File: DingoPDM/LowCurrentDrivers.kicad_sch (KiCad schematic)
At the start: 0 parts

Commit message: V5 As Built
-Changed ADS1015 to MAX11613EUA+T due to supply issues
-Changed PCB to match JLCPCB 2oz rules
-Changed ON_SW input to 12V switched
-Switched to TagConnect TC2030
-Changed pin positions of GND, IN1, IN2
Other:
- title: (none) -> Dingo_PDM
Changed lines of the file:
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@@
 (kicad_sch (version 20230121) (generator eeschema)
   (paper "A4")
+  (title_block
+    (title "Dingo_PDM")
+    (date "2023-02-23")
+    (rev "v5")
+    (comment 3 "github.com/corygrant")
+    (comment 4 "Cory Grant")
+  )
   (wire (pts (xy 52.07 74.93) (xy 57.15 74.93))
     (stroke (width 0) (type default))
@@
     (instances
       (project "DingoPDM"
-        (path "/8948e307-9174-4227-9c28-3ff885e6e83d/00000000-0000-0000-0000-00005f54bf48" (page "9"))
-      )
-    )
+        (path "/8948e307-9174-4227-9c28-3ff885e6e83d/00000000-0000-0000-0000-00005f54bf48" (page "13"))
+      )
+    )

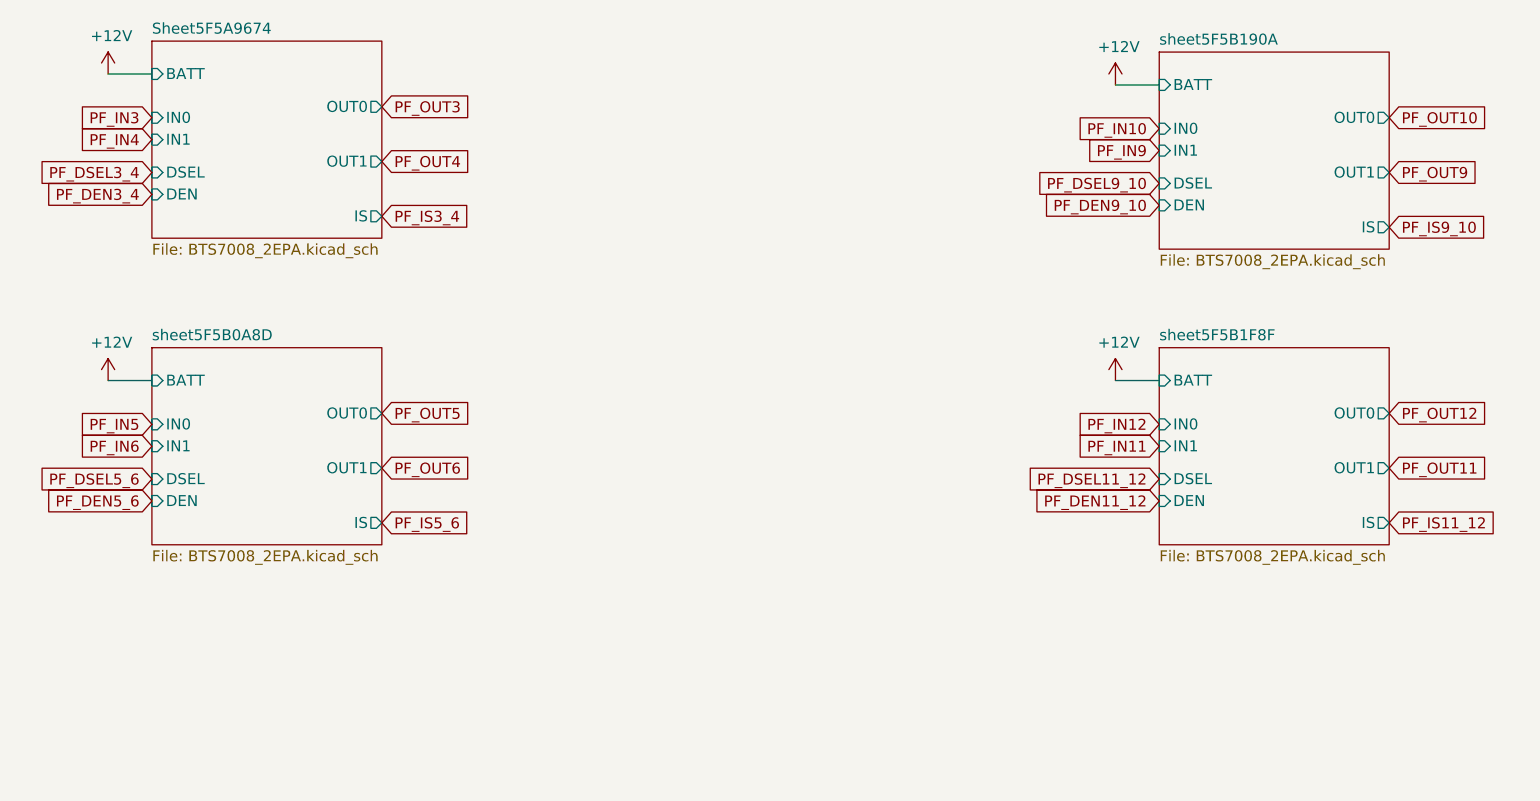
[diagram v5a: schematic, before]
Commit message: Redesigned to a smaller unit
4x high current, 2x med current, 4x low current, 2x digital inputs
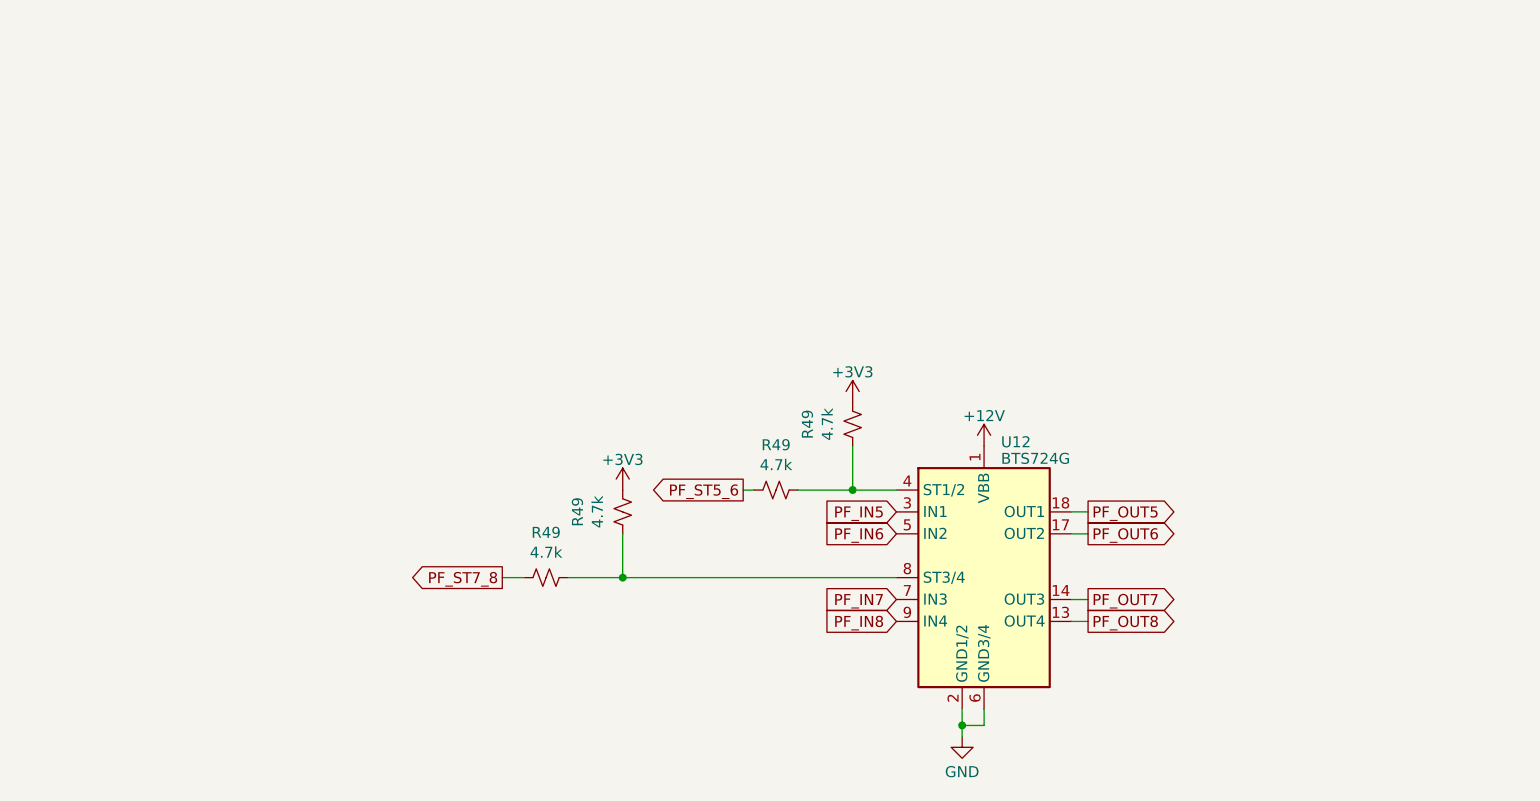
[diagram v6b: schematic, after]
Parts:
- added R49 (x4): 4.7k, Resistor_SMD:R_0805_2012Metric, symbol Device:R_Small_US
- added U12: BTS724G, Package_SO:Infineon_PG-DSO-20-32, symbol Power_Management:BTS724G
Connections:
- net +12V: now also U12.1 (VBB), U12.10 (VBB), U12.11 (VBB), U12.12 (VBB), U12.15 (VBB), U12.16 (VBB), U12.19 (VBB), U12.20 (VBB)
- net PF_IN5: now also U12.3 (IN1)
- net PF_IN6: now also U12.5 (IN2)
- net PF_OUT5: now also U12.18 (OUT1)
- net PF_OUT6: now also U12.17 (OUT2)
- new net: R49.1, R49.2, U12.8 (ST3/4)
- new net: R49.1, R49.2, U12.4 (ST1/2)
- new net +3V3: R49.1, R49.1
- new net GND: U12.2 (GND1/2), U12.6 (GND3/4)
- new net PF_IN7: U12.7 (IN3)
- new net PF_IN8: U12.9 (IN4)
- new net PF_OUT7: U12.14 (OUT3)
- new net PF_OUT8: U12.13 (OUT4)
- new net PF_ST5_6: R49.2
- new net PF_ST7_8: R49.2
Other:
- removed sheet Sheet5F5A9674
- removed sheet sheet5F5B0A8D
- removed sheet sheet5F5B190A
- removed sheet sheet5F5B1F8F

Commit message: Added documentation, finished and cleaned design
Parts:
- U12: Digi-Key_PN (none) -> BTS724GXUMA1CT-ND
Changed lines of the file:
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@@
   (title_block
     (title "Dingo_PDM")
-    (date "2023-04-01")
-    (rev "v5")
+    (date "2023-07-28")
+    (rev "v6")
     (comment 3 "github.com/corygrant")
     (comment 4 "Cory Grant")
@@
       (effects (font (size 1.27 1.27)) hide)
     )
+    (property "Digi-Key_PN" "BTS724GXUMA1CT-ND" (at 153.67 97.79 0)
+      (effects (font (size 1.27 1.27)) hide)
+    )
